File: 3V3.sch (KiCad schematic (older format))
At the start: 31 parts

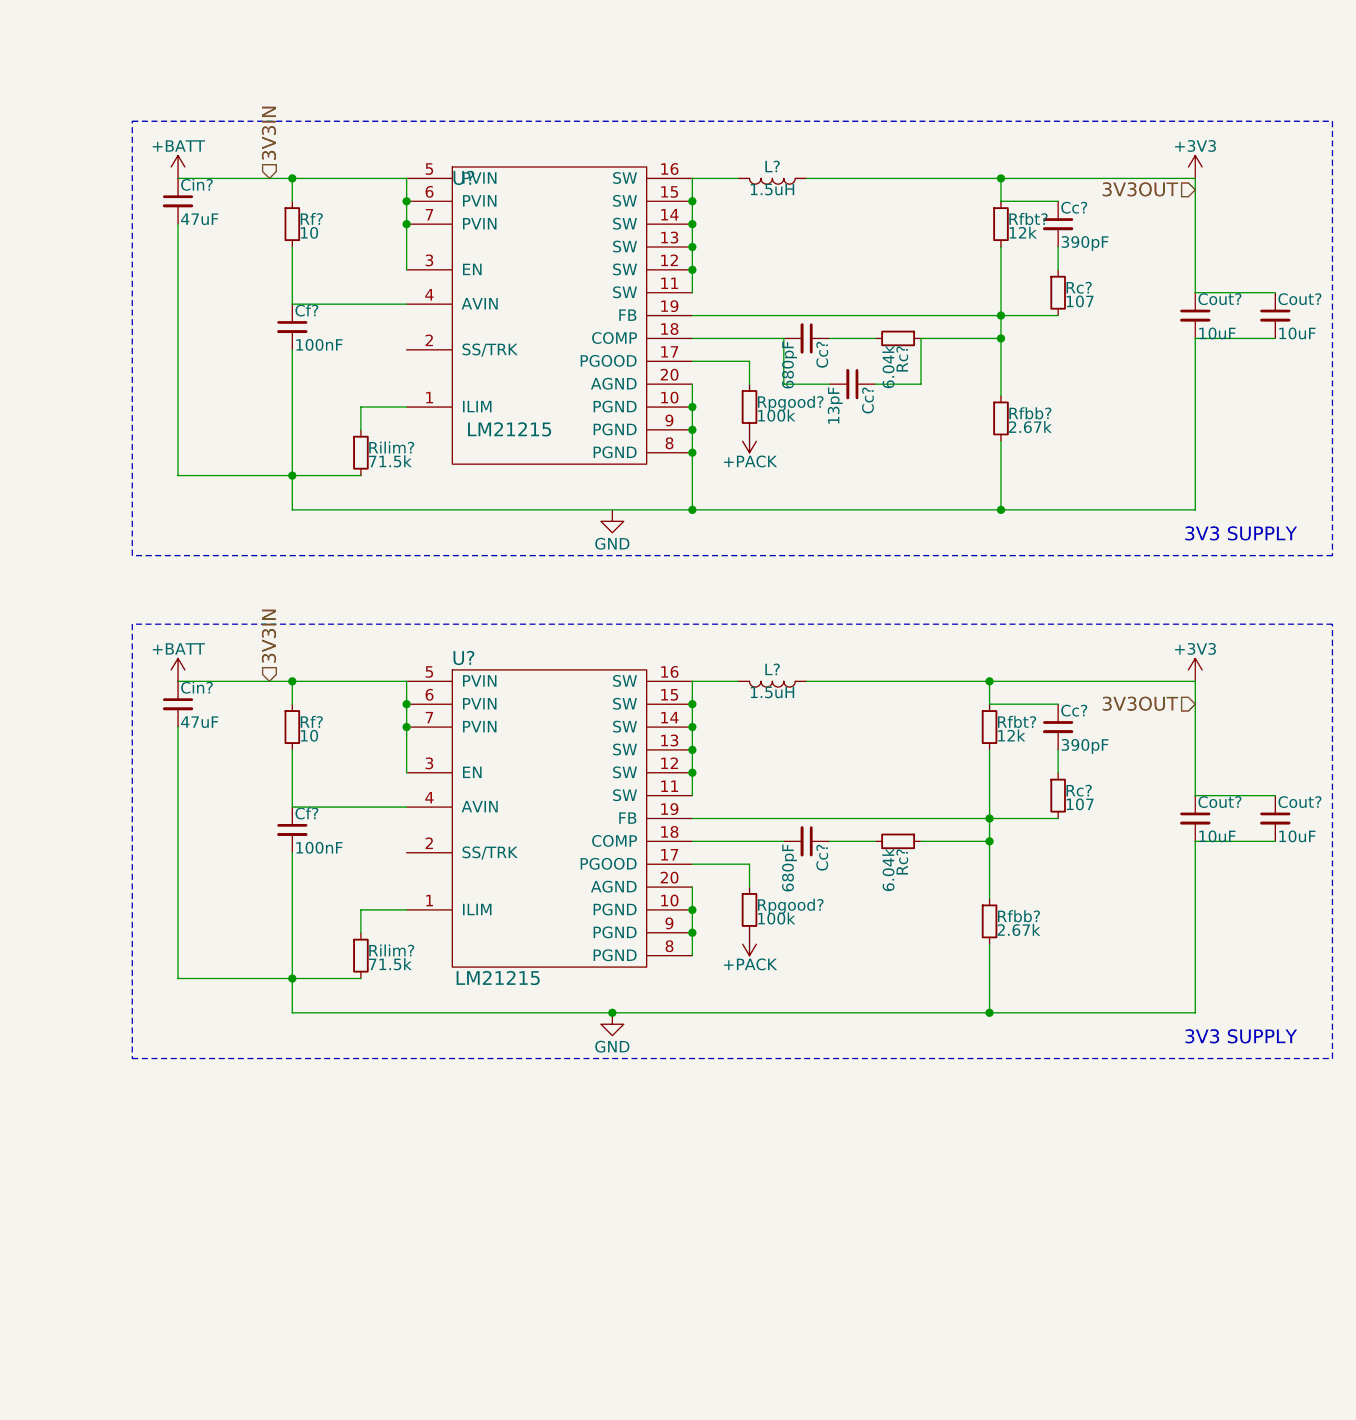
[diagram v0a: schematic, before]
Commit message: Ammetre addition
Ammetres added to 3V3 buck converter. Naming convention added for 3V3 1 and 2.
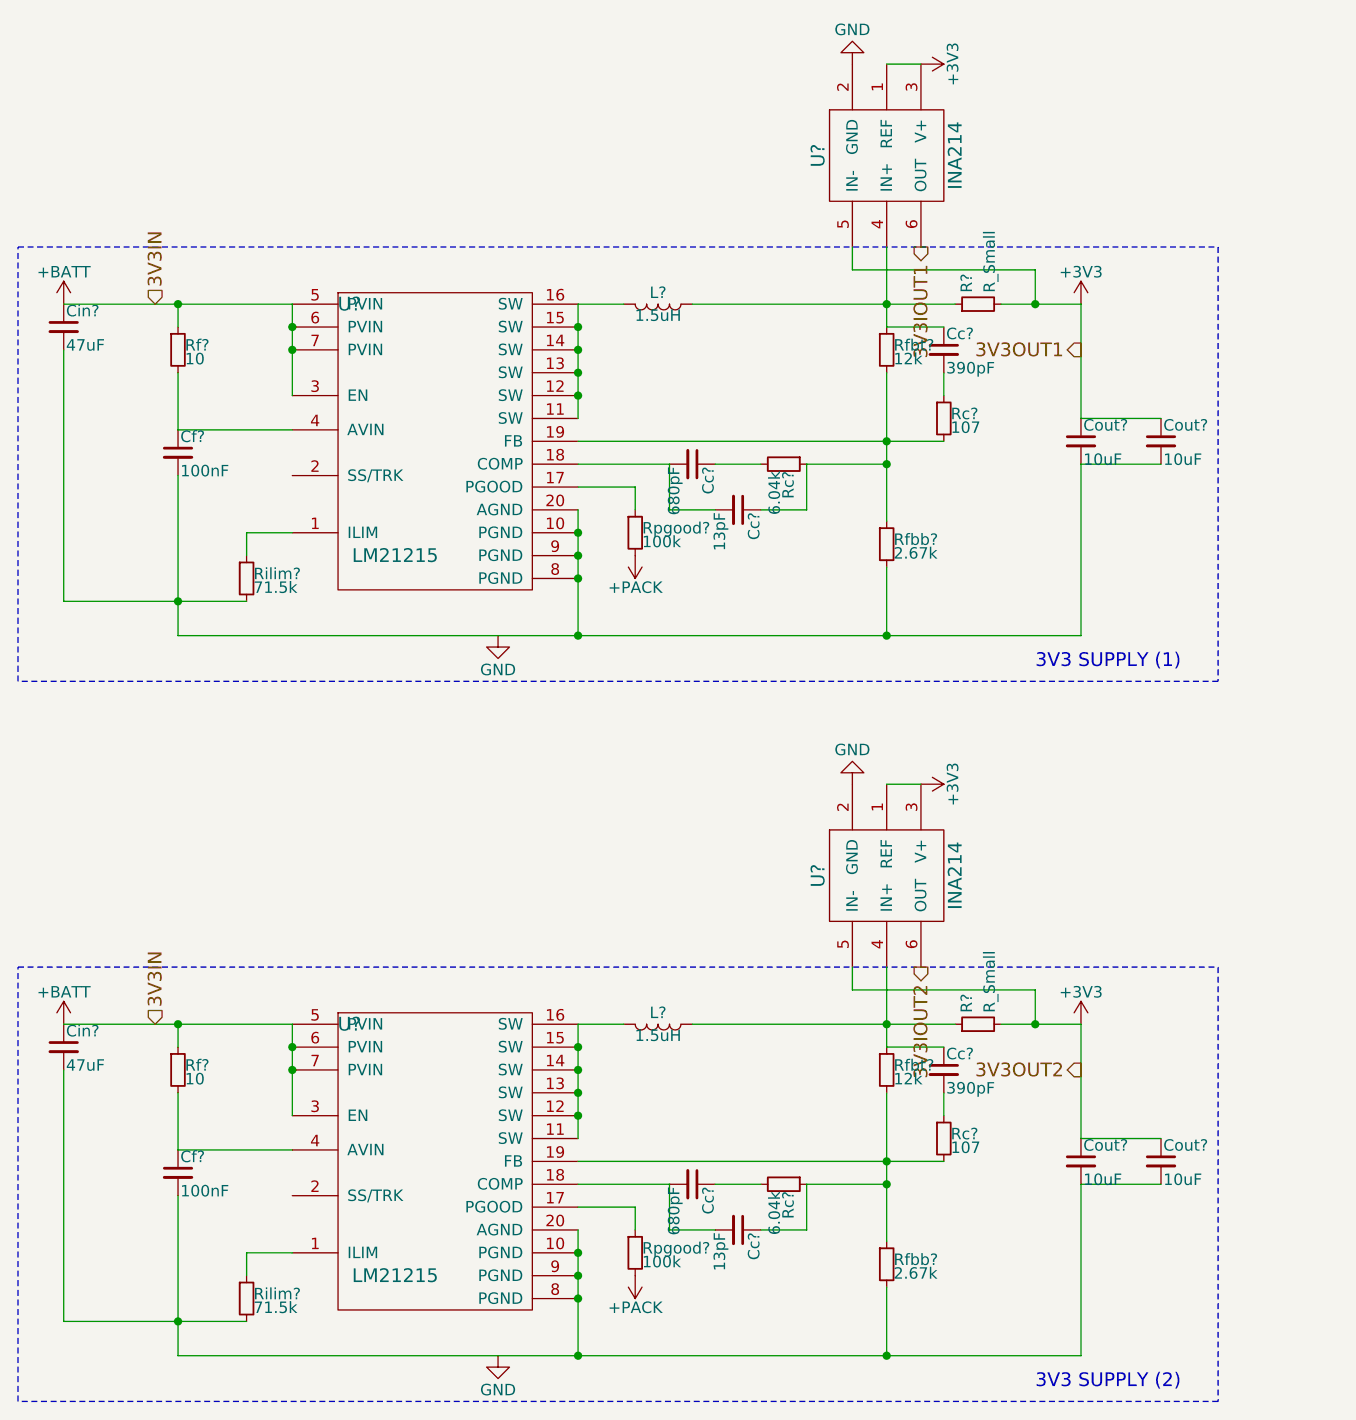
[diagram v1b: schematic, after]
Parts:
- removed Cc?: 390pF, symbol C_Small
- removed Cc?: 680pF, symbol C_Small
- removed Cf?: 100nF, symbol C_Small
- removed Cin?: 47uF, symbol C_Small
- removed Cout? (x2): 10uF, symbol C_Small
- removed L?: 1.5uH, symbol L
- removed Rc?: 107, symbol R_Small
- removed Rc?: 6.04k, symbol R_Small
- removed Rf?: 10, symbol R_Small
- removed Rfbb?: 2.67k, symbol R_Small
- removed Rfbt?: 12k, symbol R_Small
- removed Rilim?: 71.5k, symbol R_Small
- removed Rpgood?: 100k, symbol R_Small
- removed U?: LM21215, symbol LM21215
- added Cc?: 390pF, symbol C_Small
- added Cc?: 680pF, symbol C_Small
- added Cc?: 13pF, symbol C_Small
- added Cf?: 100nF, symbol C_Small
- added Cin?: 47uF, symbol C_Small
- added Cout? (x2): 10uF, symbol C_Small
- added L?: 1.5uH, symbol L
- added R? (x2): R_Small, symbol R_Small
- added Rc?: 6.04k, symbol R_Small
- added Rc?: 107, symbol R_Small
- added Rf?: 10, symbol R_Small
- added Rfbb?: 2.67k, symbol R_Small
- added Rfbt?: 12k, symbol R_Small
- added Rilim?: 71.5k, symbol R_Small
- added Rpgood?: 100k, symbol R_Small
- added U? (x2): INA214, symbol INA214
- added U?: LM21215, symbol LM21215
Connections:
- net +3V3: now also Cout?.1, Cout?.1, R?.2, R?.2, U?.1 (REF), U?.1 (REF), U?.3 (V+), U?.3 (V+), U?.5 (IN-), U?.5 (IN-); no longer Cc?.1, L?.1, Rfbt?.1
- net +BATT: now also Cin?.1, Rf?.1, U?.3 (EN), U?.5 (PVIN), U?.6 (PVIN), U?.7 (PVIN)
- net +PACK: now also Rpgood?.2
- net GND: now also U?.2 (GND), U?.2 (GND)
- new net: Cc?.1, L?.1, R?.1, Rfbt?.1, U?.4 (IN+) (x2)
- new net: Rilim?.1, U?.1 (ILIM)
- new net: Cf?.2, Cin?.2, Cout?.2, Cout?.2, Rfbb?.2, Rilim?.2, U?.10 (PGND), U?.20 (AGND), U?.8 (PGND), U?.9 (PGND)
- new net: L?.2, U?.11 (SW), U?.12 (SW), U?.13 (SW), U?.14 (SW), U?.15 (SW), U?.16 (SW)
- new net: Rpgood?.1, U?.17 (PGOOD)
- new net: Cc?.2, Cc?.2, U?.18 (COMP)
- new net: Cc?.1, Rc?.1, Rc?.2, Rfbb?.1, Rfbt?.2, U?.19 (FB)
- new net: Cf?.1, Rf?.2, U?.4 (AVIN)
- new net: Cc?.2, Rc?.1
- new net: Cc?.1, Rc?.2
- new net 3V3IOUT1: U?.6 (OUT)
- new net 3V3IOUT2: U?.6 (OUT)
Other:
- note added: "3V3 SUPPLY (1)"
- note added: "3V3 SUPPLY (2)"
- note removed: "3V3 SUPPLY"
- moved on the sheet: Cc?, Cf?, Cin?, Cout?, L?, Rc?, Rf?, Rfbb?, Rfbt?, Rilim?, Rpgood?, U?

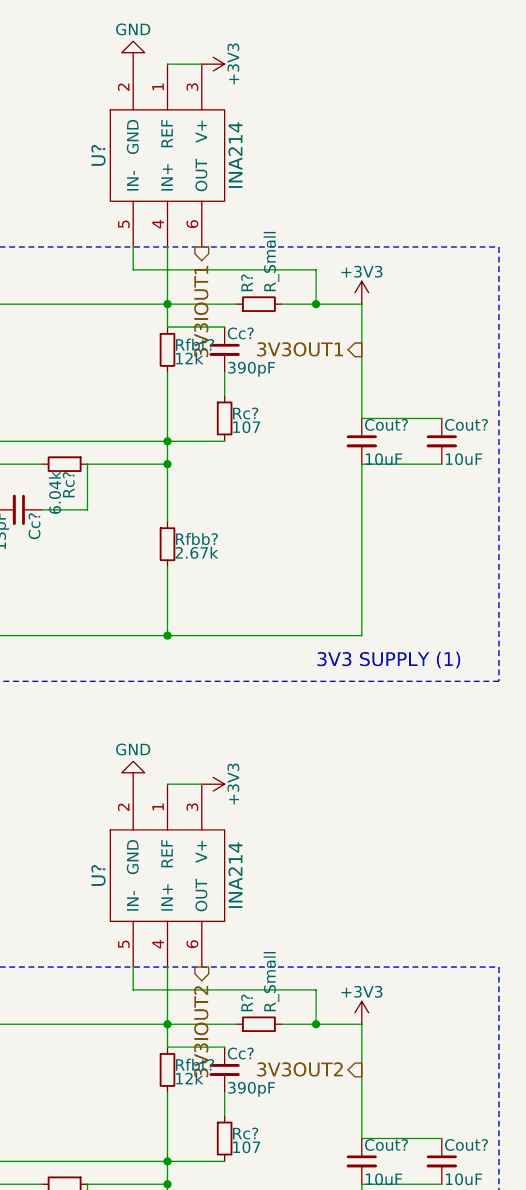
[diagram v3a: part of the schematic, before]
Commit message: Voltmeters added to 3V3 and 9V
Added 4 voltmeters. Outputs still need to be added to hierarchical sheets.
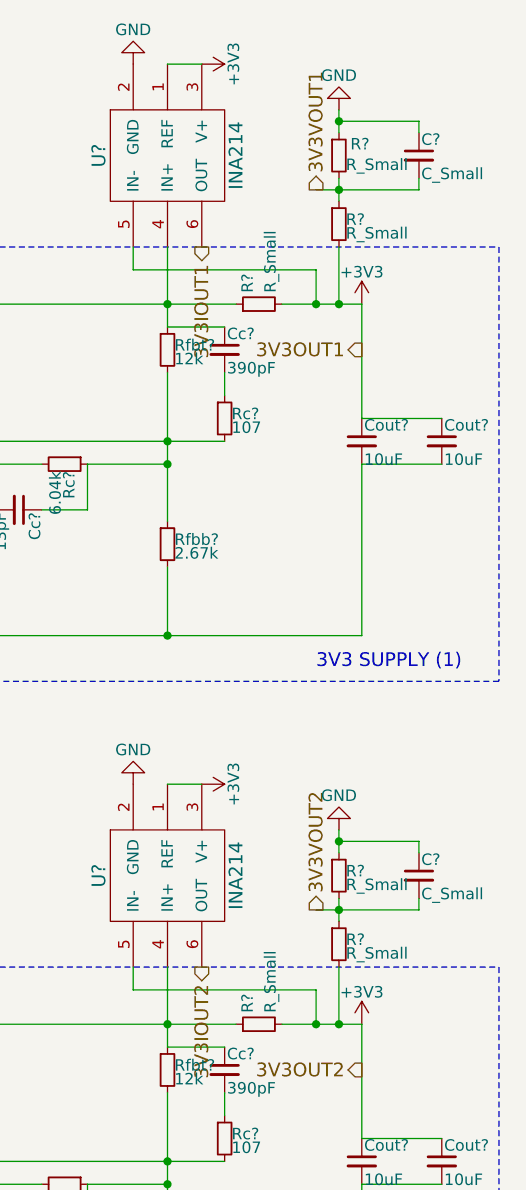
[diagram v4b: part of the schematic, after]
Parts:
- added C? (x2): C_Small, symbol C_Small
- added R? (x4): R_Small, symbol R_Small
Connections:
- net +3V3: now also R?.2, R?.2
- net GND: now also C?.1, C?.1, R?.1, R?.1
- new net 3V3VOUT1: C?.2, R?.1, R?.2
- new net 3V3VOUT2: C?.2, R?.1, R?.2
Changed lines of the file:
@@
 	0    1    1    0
 $EndComp
+Connection ~ 6250 5150
+$Comp
+L R_Small R?
+U 1 1 5A273B9A
+P 6250 4800
+F 0 "R?" H 6280 4820 50  0000 L CNN
+F 1 "R_Small" H 6280 4760 50  0000 L CNN
+F 2 "" H 6250 4800 50  0001 C CNN
+F 3 "" H 6250 4800 50  0001 C CNN
+	1    6250 4800
+	1    0    0    -1
+$EndComp
+$Comp
+L R_Small R?
+U 1 1 5A273C3B
+P 6250 4500
+F 0 "R?" H 6280 4520 50  0000 L CNN
+F 1 "R_Small" H 6280 4460 50  0000 L CNN
+F 2 "" H 6250 4500 50  0001 C CNN
+F 3 "" H 6250 4500 50  0001 C CNN
+	1    6250 4500
+	1    0    0    -1
+$EndComp
+$Comp
+L C_Small C?
+U 1 1 5A273CCB
+P 6600 4500
+F 0 "C?" H 6610 4570 50  0000 L CNN
+F 1 "C_Small" H 6610 4420 50  0000 L CNN
+F 2 "" H 6600 4500 50  0001 C CNN
+F 3 "" H 6600 4500 50  0001 C CNN
+	1    6600 4500
+	1    0    0    -1
+$EndComp
+$Comp
+L GND #PWR?
+U 1 1 5A273D55
+P 6250 4300
+F 0 "#PWR?" H 6250 4050 50  0001 C CNN
+F 1 "GND" H 6250 4150 50  0000 C CNN
+F 2 "" H 6250 4300 50  0001 C CNN
+F 3 "" H 6250 4300 50  0001 C CNN
+	1    6250 4300
+	-1   0    0    1
+$EndComp
+Wire Wire Line
+	6250 5150 6250 4900
+Wire Wire Line
+	6600 4400 6600 4350
+Wire Wire Line
+	6600 4350 6250 4350
+Wire Wire Line
+	6250 4300 6250 4400
+Connection ~ 6250 4350
+Wire Wire Line
+	6250 4600 6250 4700
+Wire Wire Line
+	6150 4650 6600 4650
+Wire Wire Line
+	6600 4650 6600 4600
+Connection ~ 6250 4650
+Text HLabel 6150 4650 1    60   Output ~ 0
+3V3VOUT2
+$Comp
+L R_Small R?
+U 1 1 5A275798
+P 6250 1650
+F 0 "R?" H 6280 1670 50  0000 L CNN
+F 1 "R_Small" H 6280 1610 50  0000 L CNN
+F 2 "" H 6250 1650 50  0001 C CNN
+F 3 "" H 6250 1650 50  0001 C CNN
+	1    6250 1650
+	1    0    0    -1
+$EndComp
+$Comp
+L R_Small R?
+U 1 1 5A27579E
+P 6250 1350
+F 0 "R?" H 6300 1400 50  0000 L CNN
+F 1 "R_Small" H 6280 1310 50  0000 L CNN
+F 2 "" H 6250 1350 50  0001 C CNN
+F 3 "" H 6250 1350 50  0001 C CNN
+	1    6250 1350
+	1    0    0    -1
+$EndComp
+$Comp
+L C_Small C?
+U 1 1 5A2757A4
+P 6600 1350
+F 0 "C?" H 6610 1420 50  0000 L CNN
+F 1 "C_Small" H 6610 1270 50  0000 L CNN
+F 2 "" H 6600 1350 50  0001 C CNN
+F 3 "" H 6600 1350 50  0001 C CNN
+	1    6600 1350
+	1    0    0    -1
+$EndComp
+$Comp
+L GND #PWR?
+U 1 1 5A2757AA
+P 6250 1150
+F 0 "#PWR?" H 6250 900 50  0001 C CNN
+F 1 "GND" H 6250 1000 50  0000 C CNN
+F 2 "" H 6250 1150 50  0001 C CNN
+F 3 "" H 6250 1150 50  0001 C CNN
+	1    6250 1150
+	-1   0    0    1
+$EndComp
+Wire Wire Line
+	6600 1250 6600 1200
+Wire Wire Line
+	6600 1200 6250 1200
+Wire Wire Line
+	6250 1150 6250 1250
+Connection ~ 6250 1200
+Wire Wire Line
+	6250 1450 6250 1550
+Wire Wire Line
+	6150 1500 6600 1500
+Wire Wire Line
+	6600 1500 6600 1450
+Connection ~ 6250 1500
+Text HLabel 6150 1500 1    60   Output ~ 0
+3V3VOUT1
+Wire Wire Line
+	6250 2000 6250 1750
+Connection ~ 6250 2000
 $EndSCHEMATC

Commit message: PCB layout as of 2018-02-07
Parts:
- U10, U11: renamed from U?; footprint (none) -> Housings_SSOP:HTSSOP-20-1EP_4.4x6.5mm_Pitch0.65mm_ThermalPad
- gave numbers to parts that had none: 40
